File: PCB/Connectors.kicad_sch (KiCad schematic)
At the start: 13 parts, among them J1 CAN SOCKET, J11 BTN1, J12 FAN1, J15 SWD Header, J2 EXTERNAL POWER, J3 BATTERY POWER, J4 STEP_MOTOR_1, J5 STEP_MOTOR_2, J6 STEP_MOTOR_3, J7 STEP_MOTOR_4, J8 STEP_MOTOR_5, J9 STEP_MOTOR_6

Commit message: Minor Schematic tweaks like - Adding pull up resistors to the spare GPIO pins - Renaming some Global Labels - Labeling all the pins on the STM32 correctly
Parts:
- added R6, R7: 10kR, Resistor_SMD:R_0402_1005Metric, symbol Device:R
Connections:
- net +3V3: now also R6.1, R7.1; no longer J15.3 (Pin_3)
- net GPIO_EXTRN1: now also R7.2
- net GPIO_EXTRN2: now also R6.2
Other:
- moved on the sheet: J11

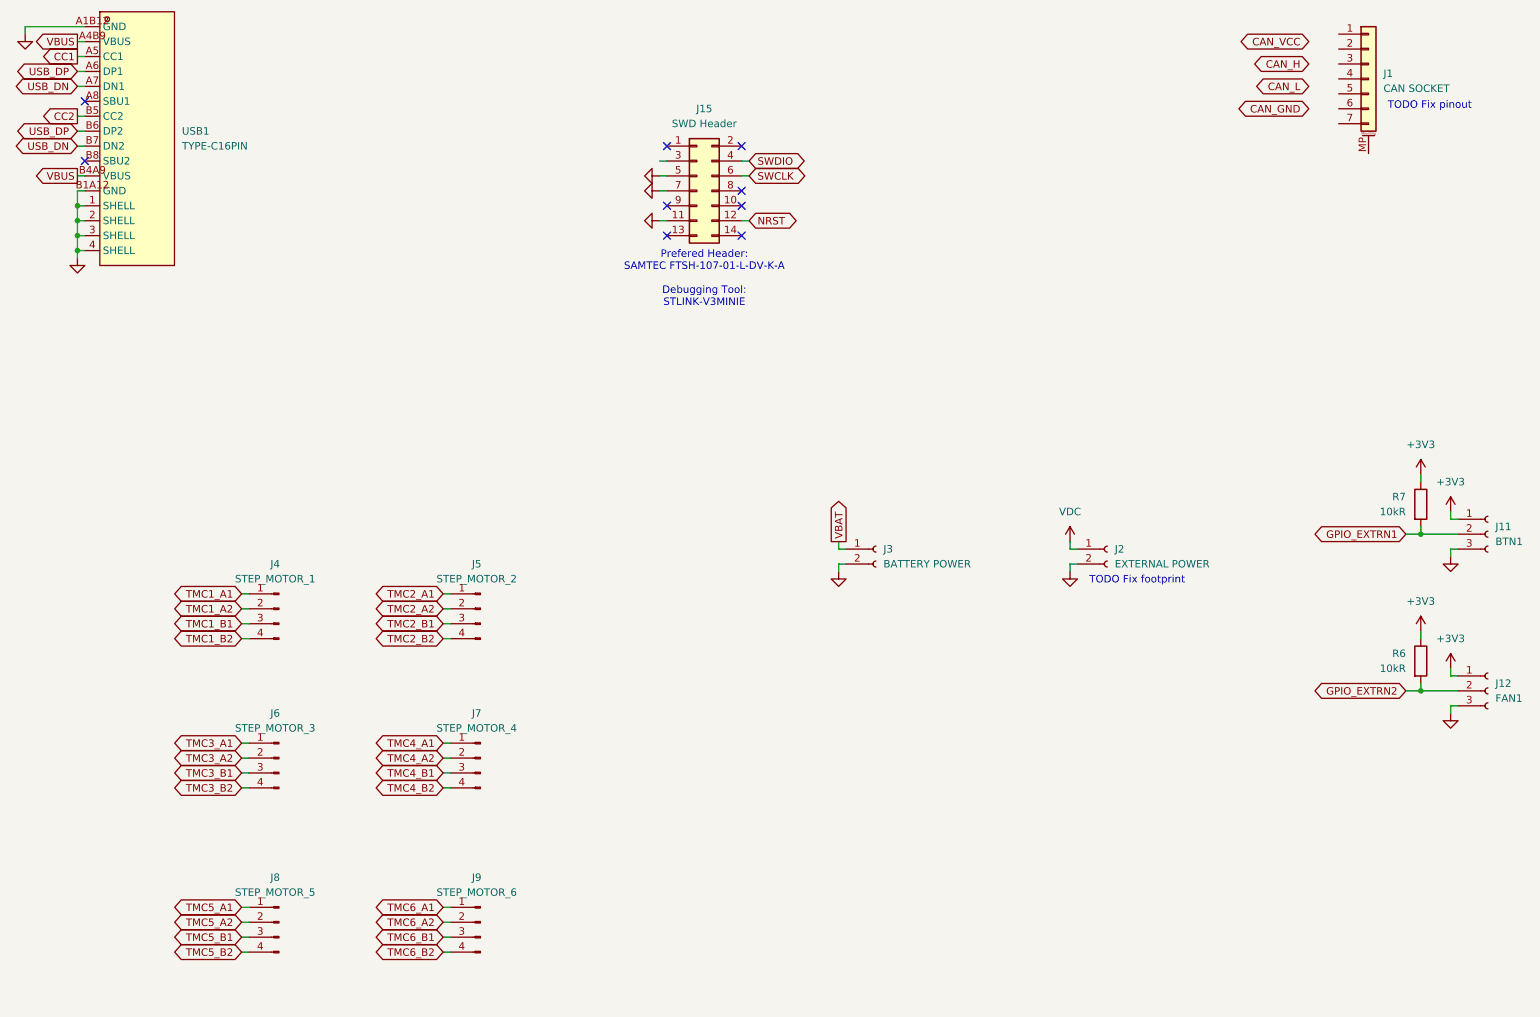
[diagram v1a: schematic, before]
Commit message: Improved Protection and Board Testability - Added power rail protection and decoupling for stepper motor noise environment - Added TVS, bulk caps and fuse upgrade on 24V rail - Added test pads for bring-up and debugging
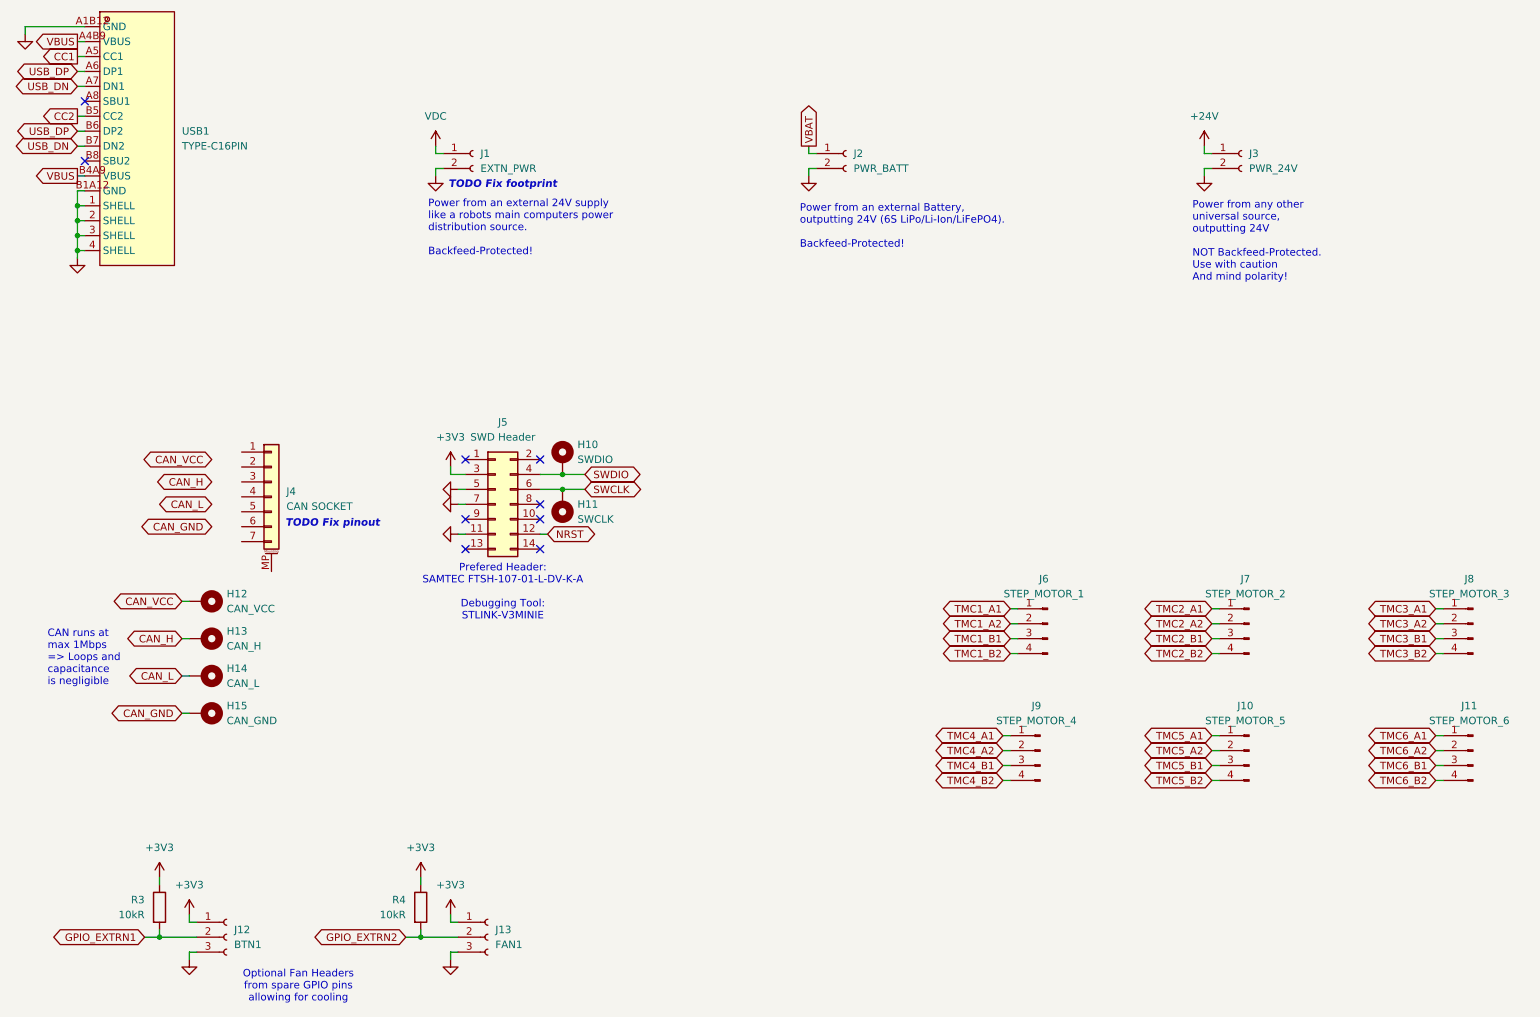
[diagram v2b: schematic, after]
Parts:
- added H10: SWDIO, TestPoint:TestPoint_Pad_D1.0mm, symbol Mechanical:MountingHole_Pad
- added H11: SWCLK, TestPoint:TestPoint_Pad_D1.0mm, symbol Mechanical:MountingHole_Pad
- added H12: CAN_VCC, TestPoint:TestPoint_Pad_D2.0mm, symbol Mechanical:MountingHole_Pad
- added H13: CAN_H, TestPoint:TestPoint_Pad_D1.0mm, symbol Mechanical:MountingHole_Pad
- added H14: CAN_L, TestPoint:TestPoint_Pad_D1.0mm, symbol Mechanical:MountingHole_Pad
- added H15: CAN_GND, TestPoint:TestPoint_Pad_D2.0mm, symbol Mechanical:MountingHole_Pad
- added J3: PWR_24V, TerminalBlock:TerminalBlock_MaiXu_MX126-5.0-02P_1x02_P5.00mm, symbol Connector:Conn_01x02_Socket
- J1: renamed from J2; value EXTERNAL POWER -> EXTN_PWR
- J2: renamed from J3; value BATTERY POWER -> PWR_BATT
- renumbered J8 to J10, J9 to J11, J11 to J12, J12 to J13, J1 to J4, J15 to J5, J4 to J6, J5 to J7, J6 to J8, J7 to J9, R7 to R3, R6 to R4
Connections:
- net +3V3: now also J5.3 (Pin_3)
- net CAN_GND: now also H15.1
- net CAN_H: now also H13.1
- net CAN_L: now also H14.1
- net CAN_VCC: now also H12.1
- net GND: now also J3.2 (Pin_2)
- net SWCLK: now also H11.1
- net SWDIO: now also H10.1
- new net +24V: J3.1 (Pin_1)
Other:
- note added: "CAN runs at max 1Mbps => Loops and capacitance is negligible"
- note added: "Optional Fan Headers from spare GPIO pins allowing for cooling"
- note added: "Power from an external 24V supply like a robots main computers power distribution source. Backfeed-Protected!"
- note added: "Power from an external Battery, outputting 24V (6S LiPo/Li-Ion/LiFePO4). Backfeed-Protected!"
- note added: "Power from any other universal source, outputting 24V NOT Backfeed-Protected. Use with caution And mind polarity!"
- moved on the sheet: J1, J10, J11, J12, J13, J2, J4, J5, J6, J7, J8, J9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

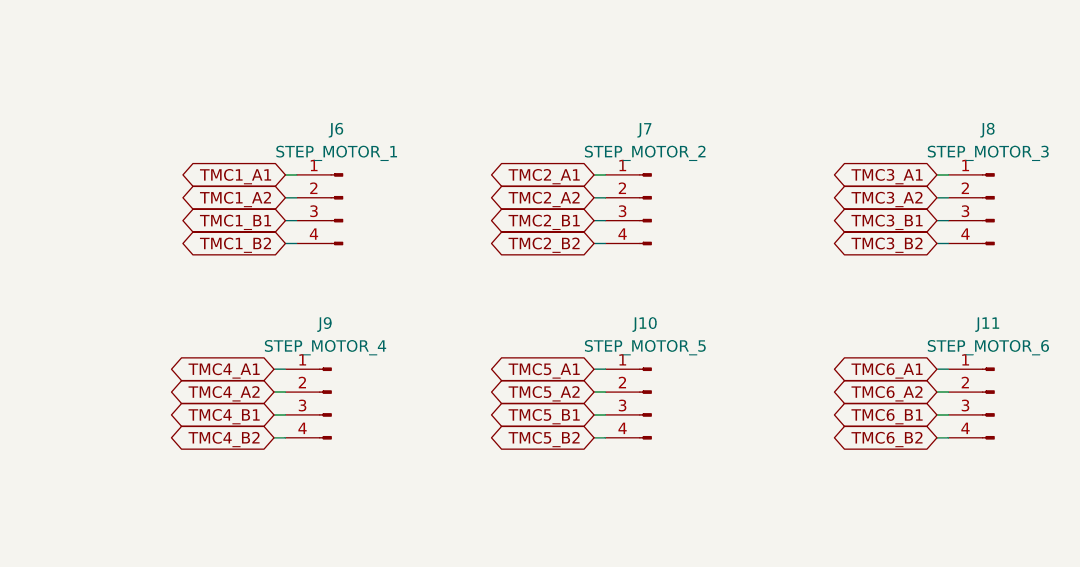
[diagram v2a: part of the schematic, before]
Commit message: PCB Layout: Initial TMC2209 driver cluster layout
- Defined netclasses for 24V, Stepper Motor, 3V3, 5V and Signal
- Decided on 4-layer stackup: Signal / GND / Power / Signal
- Routed high current motor output traces with tapered zone fills
- Placed and routed VS decoupling caps (100nF, 1uF, 47uF electrolytic)
- Routed sense resistors with dedicated GND vias per resistor
- Routed BRA/BRB via bottom layer with perpendicular crossing under motor traces
- Planned +24V / +3V3 split power plane on L3
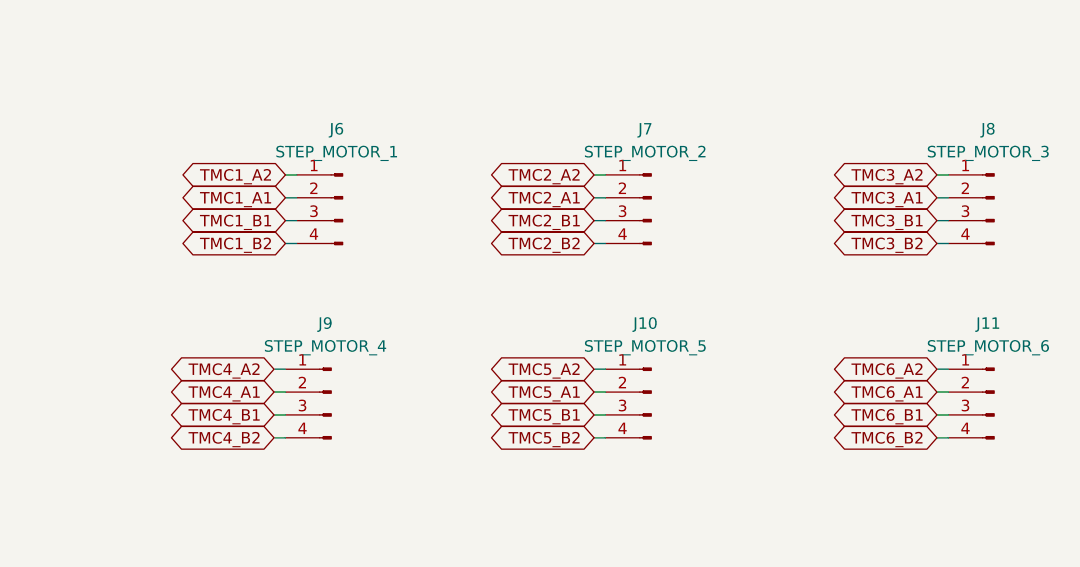
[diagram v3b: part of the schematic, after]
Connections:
- net TMC1_A1: now also J6.2 (Pin_2); no longer J6.1 (Pin_1)
- net TMC1_A2: now also J6.1 (Pin_1); no longer J6.2 (Pin_2)
- net TMC2_A1: now also J7.2 (Pin_2); no longer J7.1 (Pin_1)
- net TMC2_A2: now also J7.1 (Pin_1); no longer J7.2 (Pin_2)
- net TMC3_A1: now also J8.2 (Pin_2); no longer J8.1 (Pin_1)
- net TMC3_A2: now also J8.1 (Pin_1); no longer J8.2 (Pin_2)
- net TMC4_A1: now also J9.2 (Pin_2); no longer J9.1 (Pin_1)
- net TMC4_A2: now also J9.1 (Pin_1); no longer J9.2 (Pin_2)
- net TMC5_A1: now also J10.2 (Pin_2); no longer J10.1 (Pin_1)
- net TMC5_A2: now also J10.1 (Pin_1); no longer J10.2 (Pin_2)
- net TMC6_A1: now also J11.2 (Pin_2); no longer J11.1 (Pin_1)
- net TMC6_A2: now also J11.1 (Pin_1); no longer J11.2 (Pin_2)

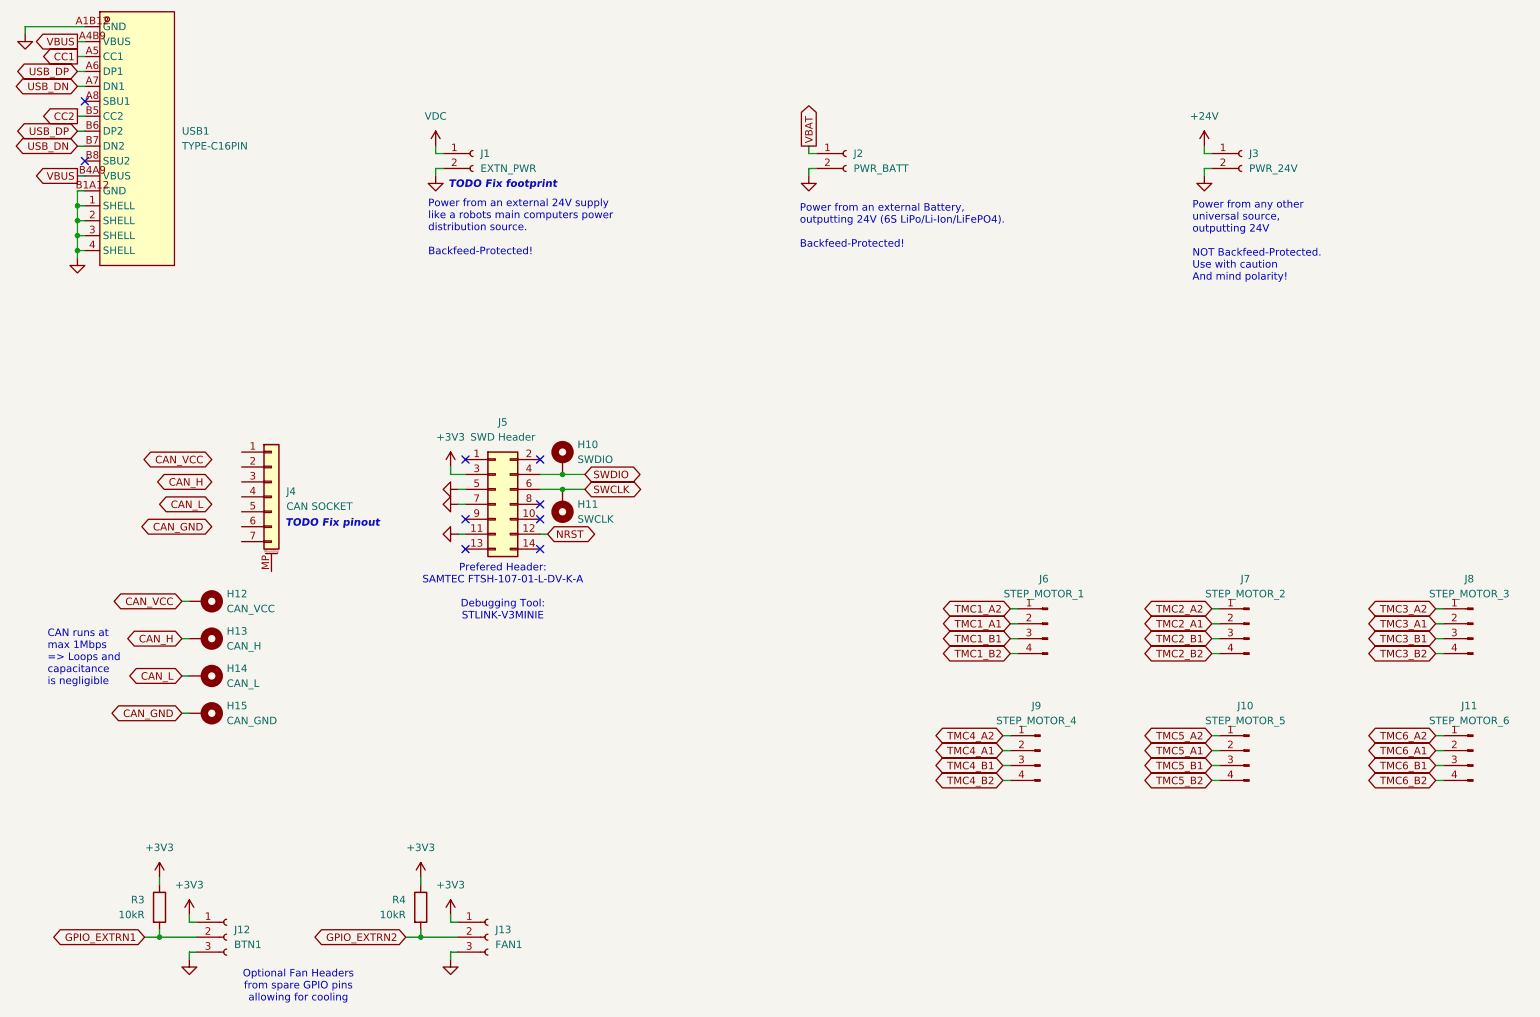
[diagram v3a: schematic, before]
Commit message: Started laying out the PCB - Decided for a square-shaped board - Split Motor Controllers on top and bottom - Split Power Plane (+3V3 on logic side, +24V on motor side) - Roughly layed out the board entirely - Reconsidered my life choises (got sick)
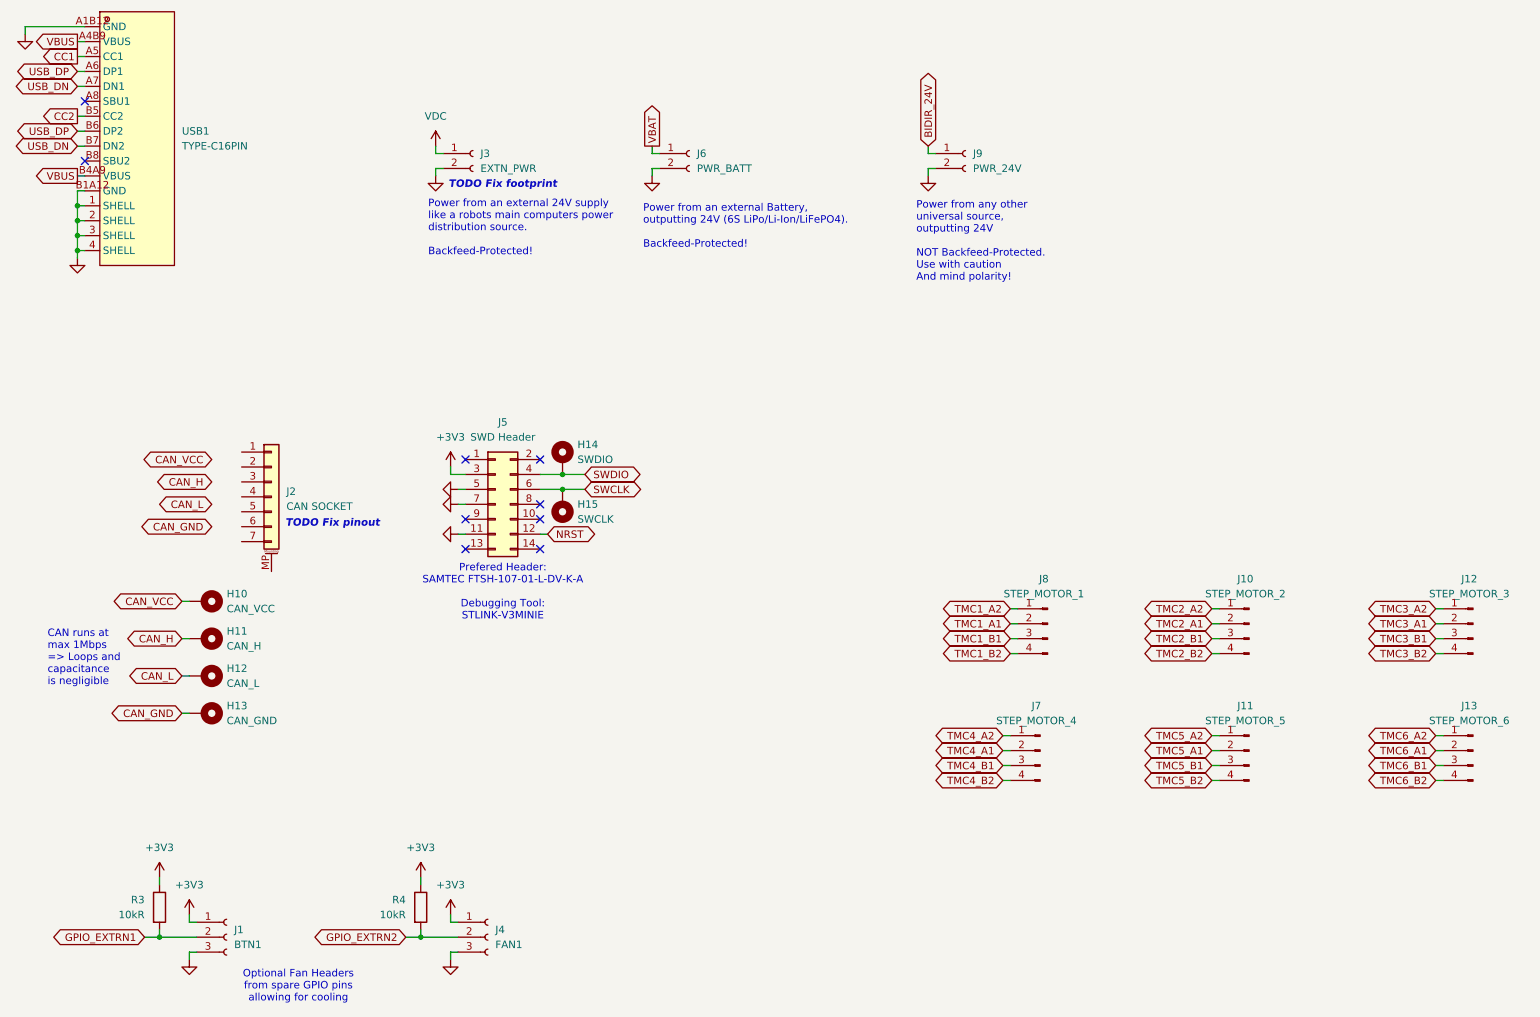
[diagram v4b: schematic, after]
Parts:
- renumbered H12 to H10, H13 to H11, H14 to H12, H15 to H13, H10 to H14, H11 to H15, J12 to J1, J7 to J10, J10 to J11, J8 to J12, J11 to J13, J4 to J2, J1 to J3, J13 to J4, J2 to J6, J9 to J7, J6 to J8, J3 to J9
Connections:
- net +24V renamed BIDIR_24V
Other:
- moved on the sheet: J6, J9

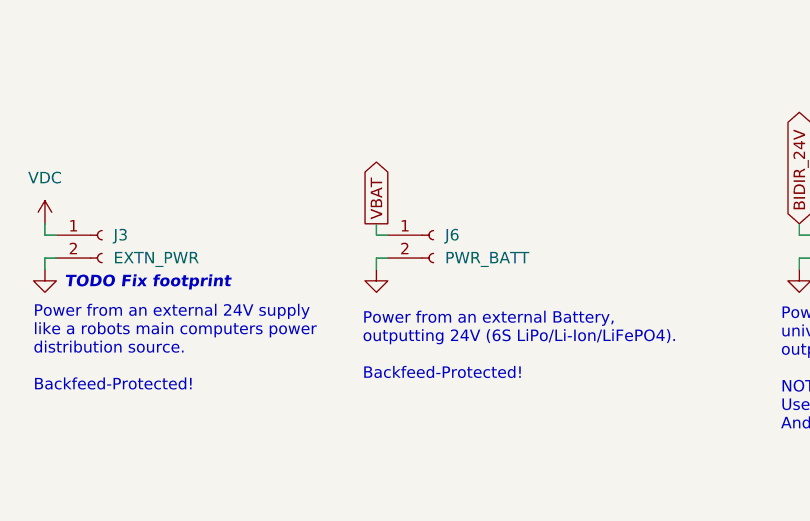
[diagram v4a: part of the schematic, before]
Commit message: Continued PCB Development - Routed MCU decoupeling and Isolated Crystal - Routed LDO Buck converter (VBUS (+5V) -> +3V3) - Routed Buck Converter (+24V -> +3V3) needs review (U2-pin1-GND) - Started Routing TMC2209 to their terminal blocks - Noticed issue with Stepper Lines coupeling back into +24V - TODO: Move Motor Input farther inside and add grounding isolation - Fixed Polariy mismatch with J3 (XT60 Battery Connector)
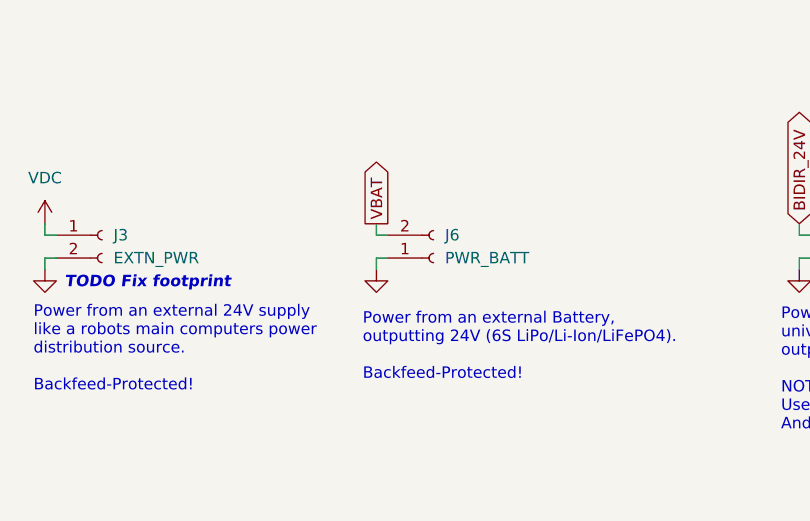
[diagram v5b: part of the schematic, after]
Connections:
- net GND: now also J6.1 (Pin_1); no longer J6.2 (Pin_2)
- net VBAT: now also J6.2 (Pin_2); no longer J6.1 (Pin_1)
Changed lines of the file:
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@@
 	)
 	(symbol
+		(lib_name "Conn_01x02_Socket_2")
 		(lib_id "Connector:Conn_01x02_Socket")
 		(at 134.62 43.18 0)
@@
 	)
 	(symbol
+		(lib_name "Conn_01x02_Socket_1")
 		(lib_id "Connector:Conn_01x02_Socket")
 		(at 97.79 43.18 0)
